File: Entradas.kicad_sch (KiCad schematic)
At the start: 19 parts

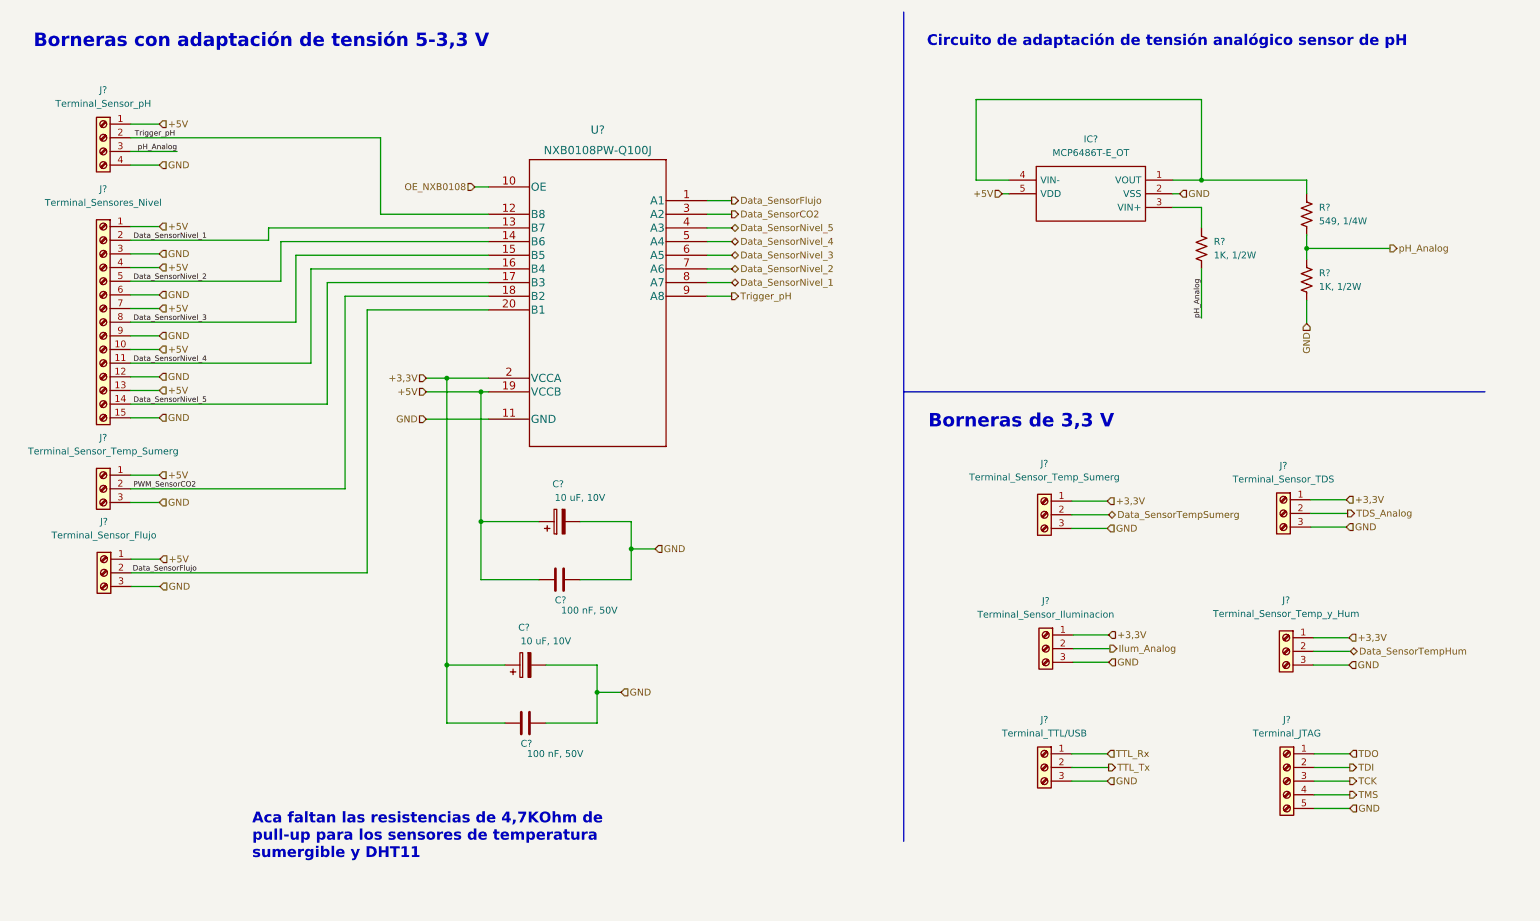
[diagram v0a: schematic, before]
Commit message: Modificación de posición de circ. filtrado y circ. de adaptación de tensión
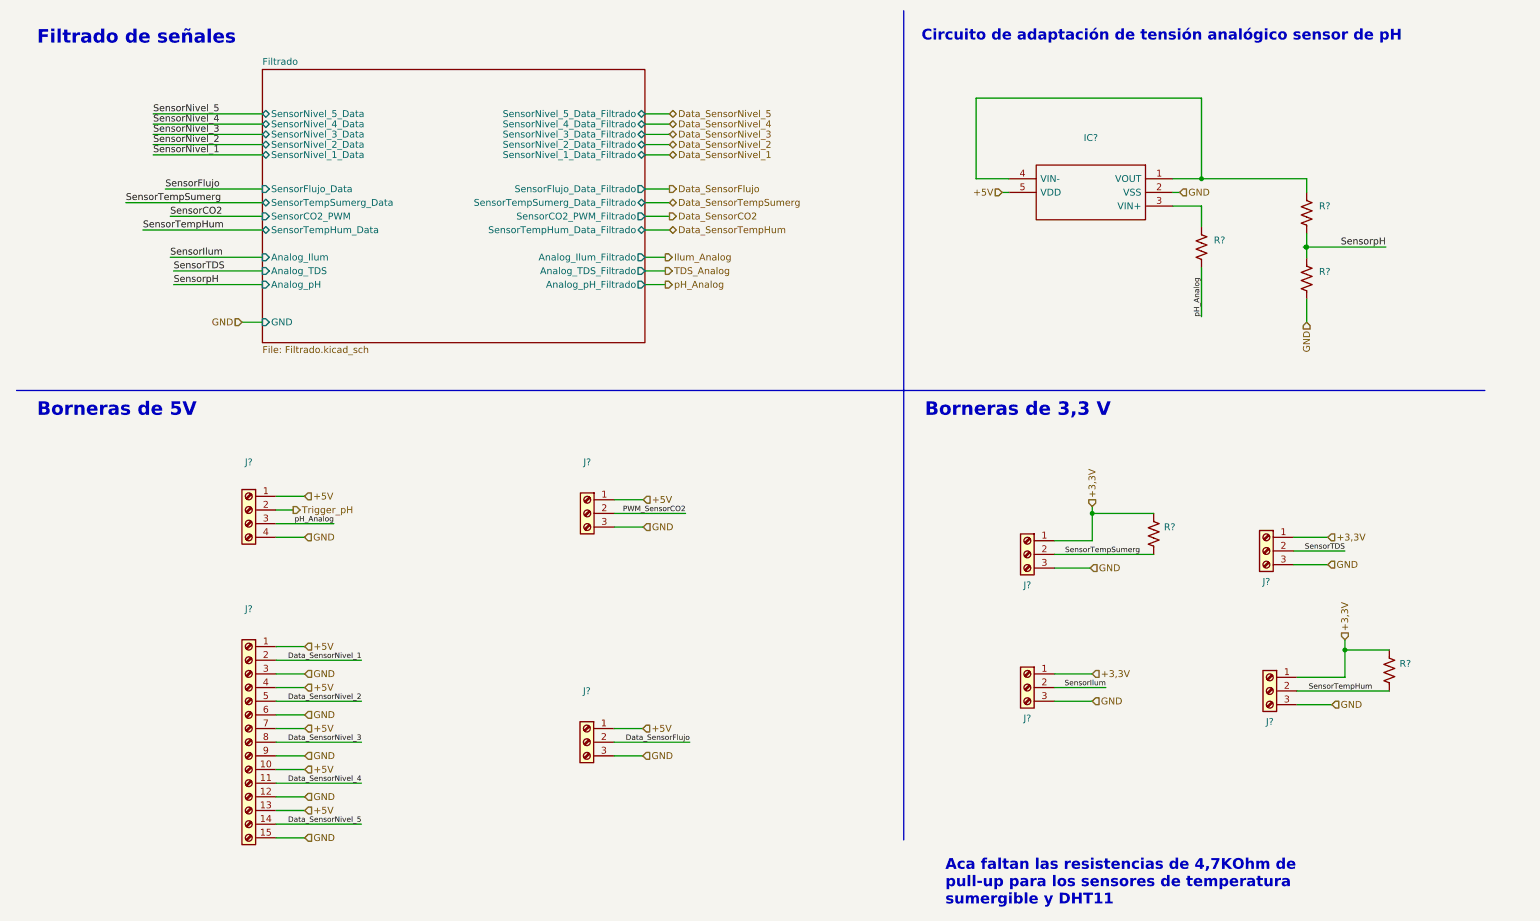
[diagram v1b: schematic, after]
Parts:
- removed C? (x2): 100 nF, 50V, symbol Device:C
- removed C? (x2): 10 uF, 10V, symbol Device:C_Polarized
- removed IC?: MCP6486T-E_OT, SOT95P280X145-5N, symbol MCP6486T-E/OT:MCP6486T-E_OT
- removed J? (x2): Terminal_Sensor_Temp_Sumerg, symbol Connector:Screw_Terminal_01x03
- removed J?: Terminal_Sensor_Temp_y_Hum, symbol Connector:Screw_Terminal_01x03
- removed J?: Terminal_TTL/USB, symbol Connector:Screw_Terminal_01x03
- removed J?: Terminal_JTAG, symbol Connector:Screw_Terminal_01x05
- removed J?: Terminal_Sensores_Nivel, symbol Connector:Screw_Terminal_01x15
- removed J?: Terminal_Sensor_Iluminacion, symbol Connector:Screw_Terminal_01x03
- removed J?: Terminal_Sensor_TDS, symbol Connector:Screw_Terminal_01x03
- removed J?: Terminal_Sensor_pH, symbol Connector:Screw_Terminal_01x04
- removed J?: Terminal_Sensor_Flujo, symbol Connector:Screw_Terminal_01x03
- removed R? (x2): 1K, 1/2W, symbol Device:R_US
- removed R?: 549, 1/4W, symbol Device:R_US
- removed U?: NXB0108PW-Q100J, Package_SO:TSSOP-20_4.4x6.5mm_P0.65mm, symbol NXB0108PWJ:NXB0108PW-Q100J
- added IC?: (no value), symbol MCP6486T-E/OT:MCP6486T-E_OT
- added J? (x6): (no value), symbol Connector:Screw_Terminal_01x03
- added J?: (no value), symbol Connector:Screw_Terminal_01x04
- added J?: (no value), symbol Connector:Screw_Terminal_01x15
- added R? (x5): (no value), symbol Device:R_US
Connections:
- net +3,3V: now also J?.1 (Pin_1), J?.1 (Pin_1), J?.1 (Pin_1), J?.1 (Pin_1), R?.1, R?.1
- net +5V: now also IC?.5 (VDD), J?.1 (Pin_1), J?.1 (Pin_1), J?.1 (Pin_1), J?.1 (Pin_1), J?.10 (Pin_10), J?.13 (Pin_13), J?.4 (Pin_4), J?.7 (Pin_7)
- net Data_SensorFlujo: now also J?.2 (Pin_2)
- net Data_SensorNivel_1: now also J?.2 (Pin_2)
- net Data_SensorNivel_2: now also J?.5 (Pin_5)
- net Data_SensorNivel_3: now also J?.8 (Pin_8)
- net Data_SensorNivel_4: now also J?.11 (Pin_11)
- net Data_SensorNivel_5: now also J?.14 (Pin_14)
- net GND: now also IC?.2 (VSS), J?.12 (Pin_12), J?.15 (Pin_15), J?.3 (Pin_3), J?.3 (Pin_3), J?.3 (Pin_3), J?.3 (Pin_3), J?.3 (Pin_3), J?.3 (Pin_3), J?.3 (Pin_3), J?.4 (Pin_4), J?.6 (Pin_6), J?.9 (Pin_9), R?.2
- net PWM_SensorCO2: now also J?.2 (Pin_2)
- net Trigger_pH: now also J?.2 (Pin_2)
- net pH_Analog: now also J?.3 (Pin_3), R?.2
- new net: IC?.1 (VOUT), IC?.4 (VIN-), R?.1
- new net: IC?.3 (VIN+), R?.1
- new net SensorIlum: J?.2 (Pin_2)
- new net SensorTDS: J?.2 (Pin_2)
- new net SensorTempHum: J?.2 (Pin_2), R?.2
- new net SensorTempSumerg: J?.2 (Pin_2), R?.2
- new net SensorpH: R?.1, R?.2
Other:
- added sheet Filtrado (Filtrado.kicad_sch)
- note added: "Borneras de 5V"
- note added: "Filtrado de señales"
- note removed: "Borneras con adaptación de tensión 5-3,3 V"

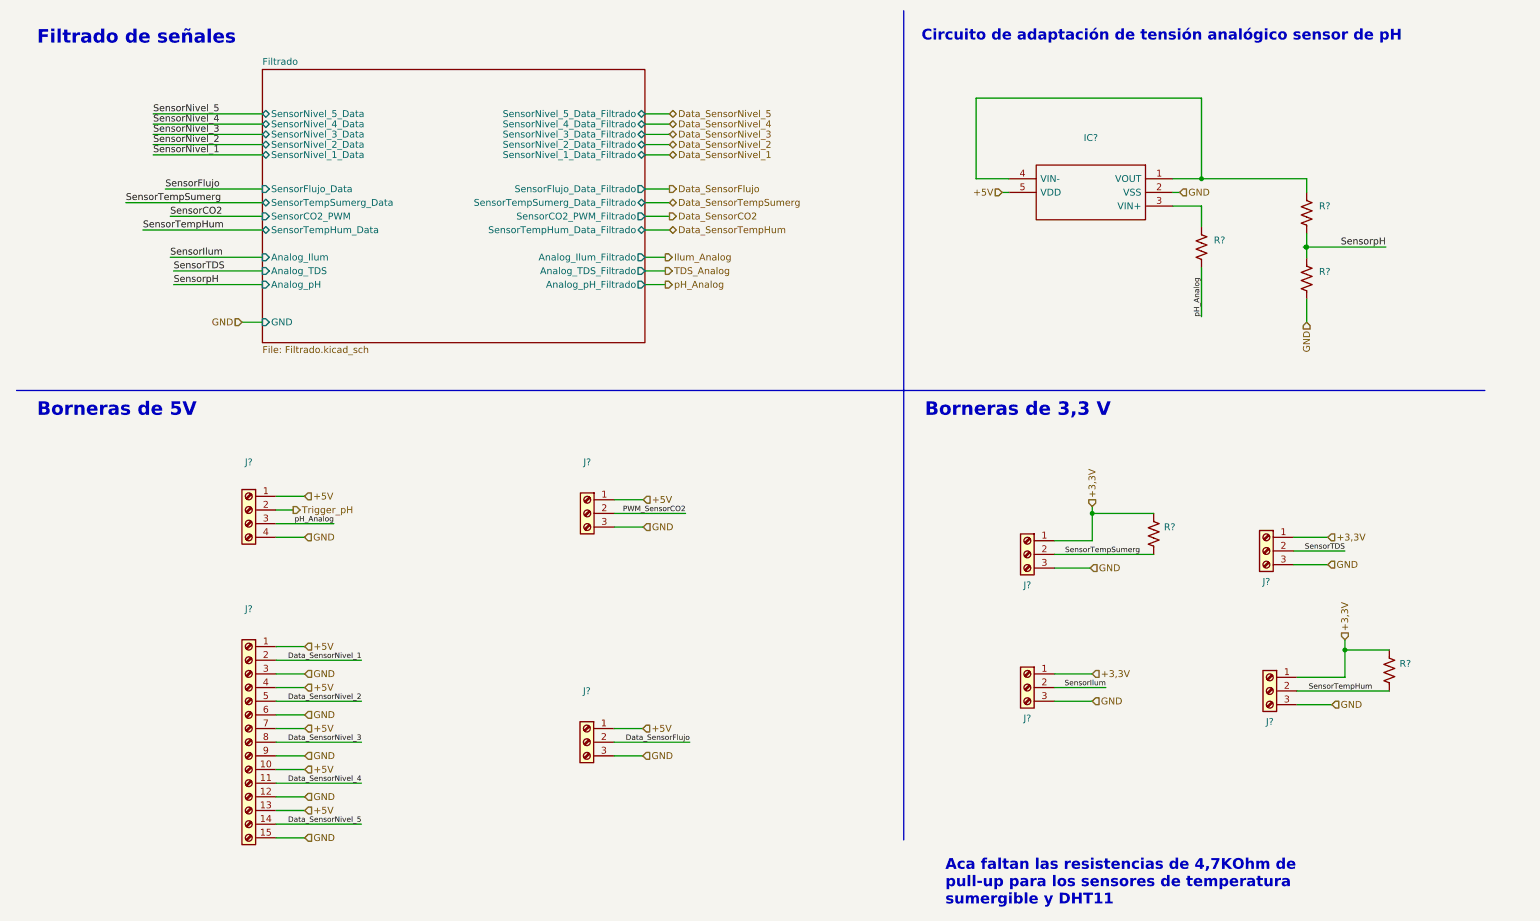
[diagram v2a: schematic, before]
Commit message: Actualización de SCH según placa industrial, y búsqueda de footprints.
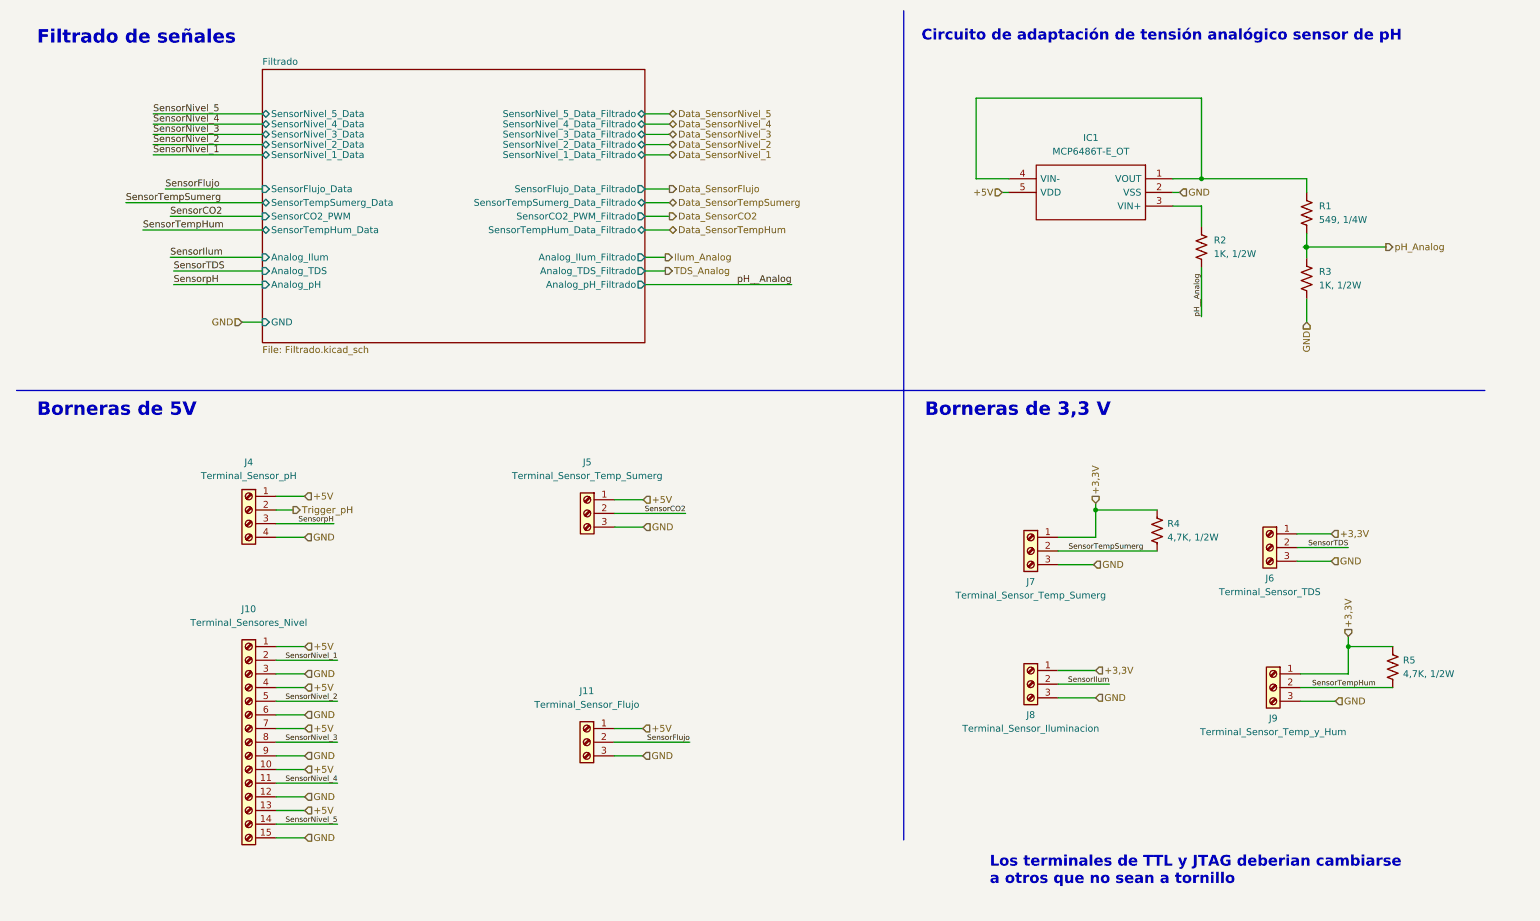
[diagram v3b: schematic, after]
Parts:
- IC1: renamed from IC?; value (none) -> MCP6486T-E_OT
- J10: renamed from J?; value (none) -> Terminal_Sensores_Nivel
- J11: renamed from J?; value (none) -> Terminal_Sensor_Flujo
- J4: renamed from J?; value (none) -> Terminal_Sensor_pH
- J5, J7: renamed from J?; value (none) -> Terminal_Sensor_Temp_Sumerg
- J6: renamed from J?; value (none) -> Terminal_Sensor_TDS
- J8: renamed from J?; value (none) -> Terminal_Sensor_Iluminacion
- J9: renamed from J?; value (none) -> Terminal_Sensor_Temp_y_Hum
- R1: renamed from R?; value (none) -> 549, 1/4W
- R2, R3: renamed from R?; value (none) -> 1K, 1/2W
- R4, R5: renamed from R?; value (none) -> 4,7K, 1/2W
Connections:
- net PWM_SensorCO2 is gone; now on net SensorCO2: J5.2 (Pin_2)
- net Data_SensorFlujo: no longer J11.2 (Pin_2)
- net Data_SensorNivel_1: no longer J10.2 (Pin_2)
- net Data_SensorNivel_2: no longer J10.5 (Pin_5)
- net Data_SensorNivel_3: no longer J10.8 (Pin_8)
- net Data_SensorNivel_4: no longer J10.11 (Pin_11)
- net Data_SensorNivel_5: no longer J10.14 (Pin_14)
- net SensorFlujo: now also J11.2 (Pin_2)
- net SensorNivel_1: now also J10.2 (Pin_2)
- net SensorNivel_2: now also J10.5 (Pin_5)
- net SensorNivel_3: now also J10.8 (Pin_8)
- net SensorNivel_4: now also J10.11 (Pin_11)
- net SensorNivel_5: now also J10.14 (Pin_14)
- net SensorpH: now also J4.3 (Pin_3); no longer R1.2, R3.1
- net pH_Analog: now also R1.2, R3.1; no longer J4.3 (Pin_3), R2.2
- new net pH__Analog: R2.2
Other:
- note added: "Los terminales de TTL y JTAG deberian cambiarse a otros que no sean a tornillo"
- note removed: "Aca faltan las resistencias de 4,7KOhm de pull-up para los sensores de temperatura sumergible y DHT11"
- moved on the sheet: J6, J7, J8, J9, R4, R5

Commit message: Fin de SCH, config de inicio para PCB
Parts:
- IC1: footprint (none) -> MCP6486T-E_OT:MCP6486RT-E&slash_OT
- J10: footprint (none) -> TB002-500-15BE:CUI_TB002-500-15BE
- J11, J5, J6, J7, J8, J9: footprint (none) -> TB002-500-03BE:SHDR3W100P0X500_1X3_1500X760X1000P
- J4: footprint (none) -> TB001-500-04BE:TB00150004BE
- R1, R2, R3, R4, R5: footprint (none) -> Resistor_SMD:R_0805_2012Metric
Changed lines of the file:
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@@
     (property "Reference" "J7" (id 0) (at 200.66 118.11 0))
     (property "Value" "Terminal_Sensor_Temp_Sumerg" (id 1) (at 200.66 120.65 0))
-    (property "Footprint" "" (id 2) (at 200.66 112.395 0)
+    (property "Footprint" "TB002-500-03BE:SHDR3W100P0X500_1X3_1500X760X1000P" (id 2) (at 200.66 112.395 0)
       (effects (font (size 1.27 1.27)) hide)
     )
@@
     (property "Reference" "J9" (id 0) (at 245.745 143.51 0))
     (property "Value" "Terminal_Sensor_Temp_y_Hum" (id 1) (at 245.745 146.05 0))
-    (property "Footprint" "" (id 2) (at 245.745 137.795 0)
+    (property "Footprint" "TB002-500-03BE:SHDR3W100P0X500_1X3_1500X760X1000P" (id 2) (at 245.745 137.795 0)
       (effects (font (size 1.27 1.27)) hide)
     )
@@
     (property "Reference" "J11" (id 0) (at 118.11 138.43 0))
     (property "Value" "Terminal_Sensor_Flujo" (id 1) (at 118.11 140.97 0))
-    (property "Footprint" "" (id 2) (at 118.11 147.955 0)
+    (property "Footprint" "TB002-500-03BE:SHDR3W100P0X500_1X3_1500X760X1000P" (id 2) (at 118.11 147.955 0)
       (effects (font (size 1.27 1.27)) hide)
     )
@@
     (property "Reference" "J8" (id 0) (at 200.66 142.875 0))
     (property "Value" "Terminal_Sensor_Iluminacion" (id 1) (at 200.66 145.415 0))
-    (property "Footprint" "" (id 2) (at 200.66 137.16 0)
+    (property "Footprint" "TB002-500-03BE:SHDR3W100P0X500_1X3_1500X760X1000P" (id 2) (at 200.66 137.16 0)
       (effects (font (size 1.27 1.27)) hide)
     )
@@
     (property "Reference" "J5" (id 0) (at 118.1862 95.885 0))
     (property "Value" "Terminal_Sensor_Temp_Sumerg" (id 1) (at 118.1862 98.425 0))
-    (property "Footprint" "" (id 2) (at 118.1862 105.41 0)
+    (property "Footprint" "TB002-500-03BE:SHDR3W100P0X500_1X3_1500X760X1000P" (id 2) (at 118.1862 105.41 0)
       (effects (font (size 1.27 1.27)) hide)
     )
@@
     (property "Reference" "J4" (id 0) (at 55.245 95.885 0))
     (property "Value" "Terminal_Sensor_pH" (id 1) (at 55.245 98.425 0))
-    (property "Footprint" "" (id 2) (at 55.245 104.775 0)
+    (property "Footprint" "TB001-500-04BE:TB00150004BE" (id 2) (at 55.245 104.775 0)
       (effects (font (size 1.27 1.27)) hide)
     )
@@
       (effects (font (size 1.27 1.27)) (justify left))
     )
-    (property "Footprint" "" (id 2) (at 225.171 108.839 90)
+    (property "Footprint" "Resistor_SMD:R_0805_2012Metric" (id 2) (at 225.171 108.839 90)
       (effects (font (size 1.27 1.27)) hide)
     )
@@
       (effects (font (size 1.27 1.27)) (justify left))
     )
-    (property "Footprint" "" (id 2) (at 252.984 49.784 90)
+    (property "Footprint" "Resistor_SMD:R_0805_2012Metric" (id 2) (at 252.984 49.784 90)
       (effects (font (size 1.27 1.27)) hide)
     )
@@
       (effects (font (size 1.27 1.27)) (justify left))
     )
-    (property "Footprint" "" (id 2) (at 268.986 134.239 90)
+    (property "Footprint" "Resistor_SMD:R_0805_2012Metric" (id 2) (at 268.986 134.239 90)
       (effects (font (size 1.27 1.27)) hide)
     )
@@
       (effects (font (size 1.27 1.27)) (justify left))
     )
-    (property "Footprint" "" (id 2) (at 252.984 61.976 90)
+    (property "Footprint" "Resistor_SMD:R_0805_2012Metric" (id 2) (at 252.984 61.976 90)
       (effects (font (size 1.27 1.27)) hide)
     )
@@
     (property "Reference" "J6" (id 0) (at 245.11 117.475 0))
     (property "Value" "Terminal_Sensor_TDS" (id 1) (at 245.11 120.015 0))
-    (property "Footprint" "" (id 2) (at 245.11 111.76 0)
+    (property "Footprint" "TB002-500-03BE:SHDR3W100P0X500_1X3_1500X760X1000P" (id 2) (at 245.11 111.76 0)
       (effects (font (size 1.27 1.27)) hide)
     )
@@
     (property "Reference" "IC1" (id 0) (at 211.836 35.56 0))
     (property "Value" "MCP6486T-E_OT" (id 1) (at 211.836 38.1 0))
-    (property "Footprint" "" (id 2) (at 200.406 40.64 0)
+    (property "Footprint" "MCP6486T-E_OT:MCP6486RT-E&slash_OT" (id 2) (at 200.406 40.64 0)
       (effects (font (size 1.27 1.27)) (justify left) hide)
     )
@@
       (effects (font (size 1.27 1.27)) (justify left))
     )
-    (property "Footprint" "" (id 2) (at 233.426 56.134 90)
+    (property "Footprint" "Resistor_SMD:R_0805_2012Metric" (id 2) (at 233.426 56.134 90)
       (effects (font (size 1.27 1.27)) hide)
     )
@@
     (property "Reference" "J10" (id 0) (at 55.245 123.19 0))
     (property "Value" "Terminal_Sensores_Nivel" (id 1) (at 55.245 125.73 0))
-    (property "Footprint" "" (id 2) (at 55.245 147.955 0)
-      (effects (font (size 1.27 1.27)) hide)
-    )
+    (property "Footprint" "TB002-500-15BE:CUI_TB002-500-15BE" (id 2) (at 55.245 147.955 0)
+      (effects (font (size 1.27 1.27)) hide)
+    )
